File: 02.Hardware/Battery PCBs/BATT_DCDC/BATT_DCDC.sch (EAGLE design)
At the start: 66 parts, among them K3 FLEX8, Q1 NVTFS9D6P04M8LTAG, Q2 2N7002PW, Q5 2N7002PW, U1 MCP6071T-E/OT, U3 TPS55330RTET, U7 TPIC2810D

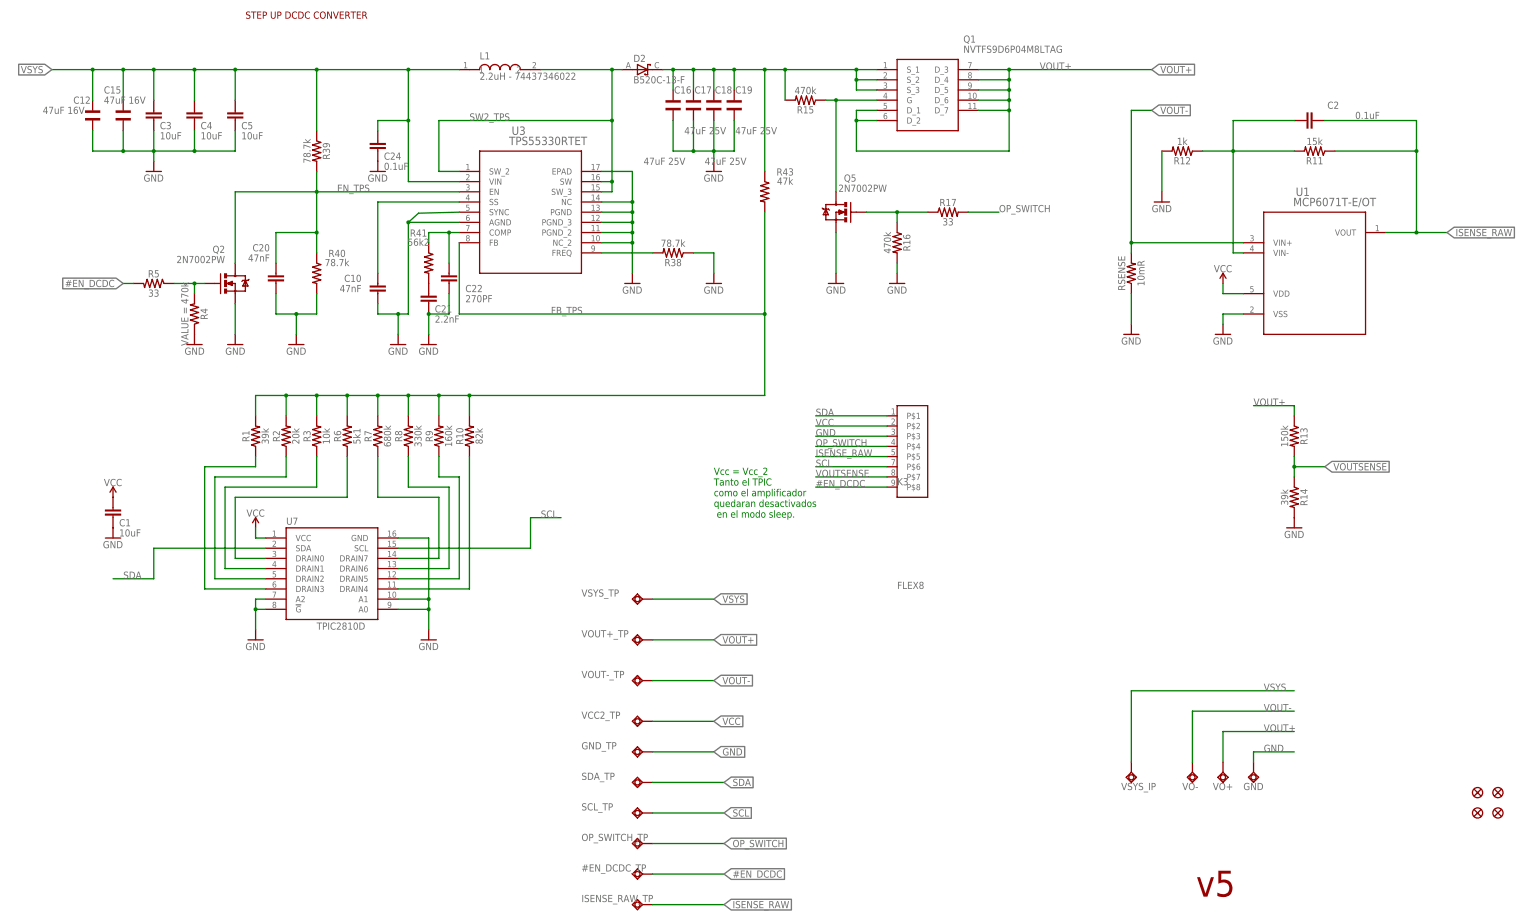
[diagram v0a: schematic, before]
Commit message: Cambios revisados con David
Revision de los pcbs de la bateria.

En el DCDC se añade un diode Clamp (bat54s) en la medicion de la tension de salida.
Actualizacion de la BOM a v8.
Documentos de Cambios de versiones
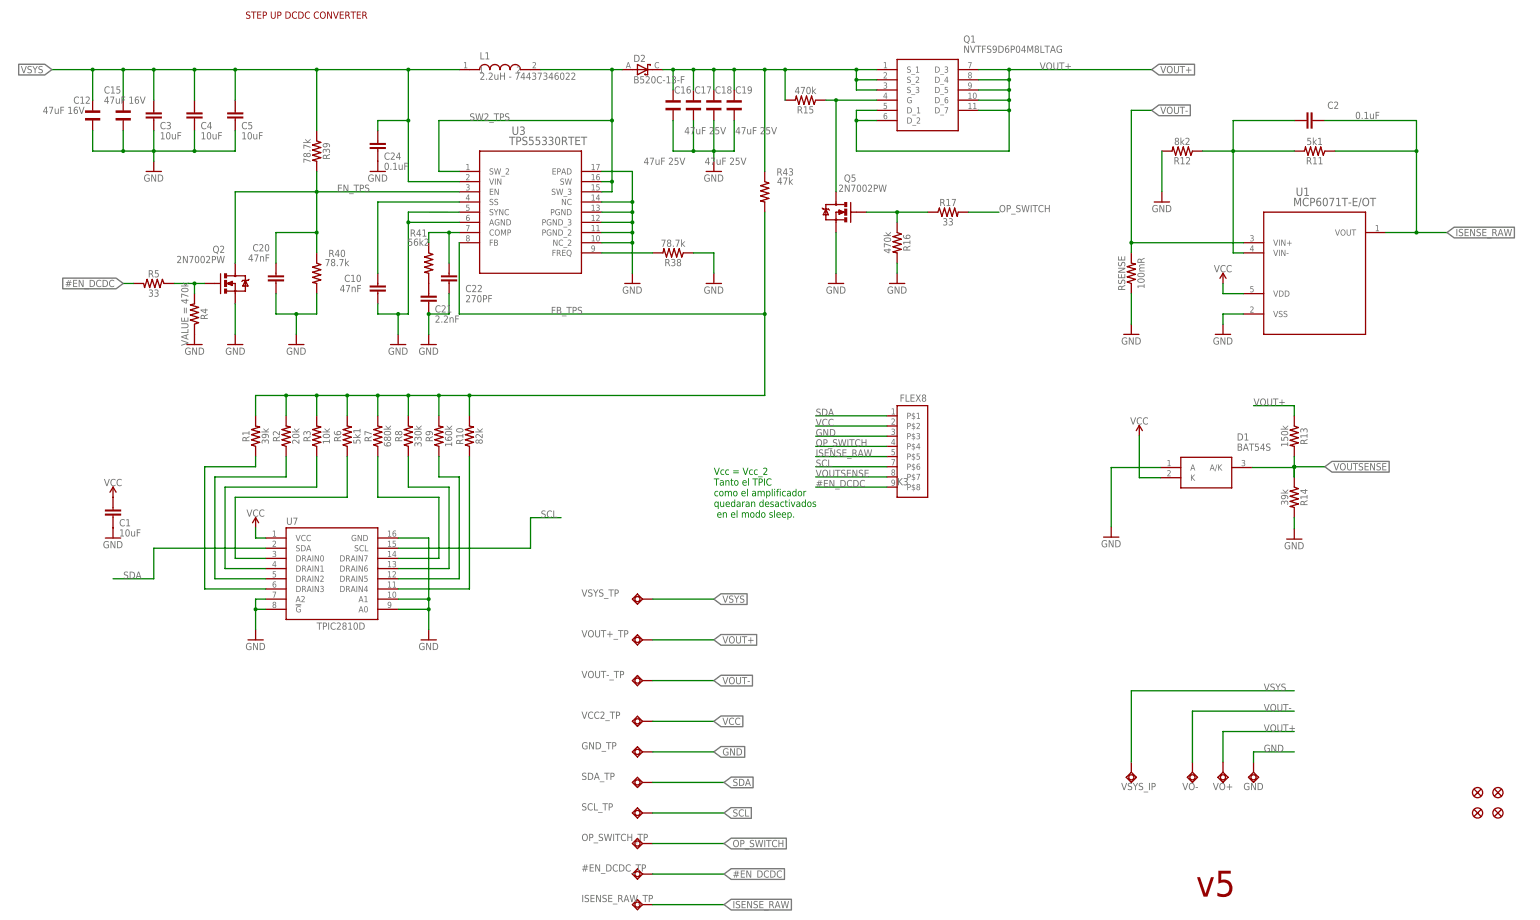
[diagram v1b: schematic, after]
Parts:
- added D1: BAT54S, BAT54S:BAT54S
- R11: value 15k -> 5k1
- R12: value 1k -> 8k2
- RSENSE: value 10mR -> 100mR
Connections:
- net GND: now also D1.A
- net VCC: now also D1.K
- net VOUTSENSE: now also D1.A/K
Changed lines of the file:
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@@
 <setting verticaltext="up"/>
 </settings>
-<grid distance="0.1" unitdist="mm" unit="mm" style="lines" multiple="1" display="no" altdistance="0.01" altunitdist="inch" altunit="inch"/>
+<grid distance="0.1" unitdist="inch" unit="inch" style="lines" multiple="1" display="no" altdistance="0.01" altunitdist="inch" altunit="inch"/>
 <layers>
 <layer number="1" name="Top" color="4" fill="1" visible="no" active="no"/>
@@
 <part name="SUPPLY2" library="SparkFun-PowerSymbols" library_urn="urn:adsk.eagle:library:530" deviceset="VCC" device=""/>
 <part name="U1" library="MCP6071" deviceset="MCP6071T-E/OT" device=""/>
-<part name="R11" library="SparkFun-Resistors" library_urn="urn:adsk.eagle:library:532" deviceset="RESISTOR" device="0402" package3d_urn="urn:adsk.eagle:package:39657/1" value="15k"/>
+<part name="R11" library="SparkFun-Resistors" library_urn="urn:adsk.eagle:library:532" deviceset="RESISTOR" device="0402" package3d_urn="urn:adsk.eagle:package:39657/1" value="5k1"/>
 <part name="FRAME2" library="microbuilder" deviceset="FRAME_A3" device=""/>
-<part name="R12" library="SparkFun-Resistors" library_urn="urn:adsk.eagle:library:532" deviceset="RESISTOR" device="0402" package3d_urn="urn:adsk.eagle:package:39657/1" value="1k"/>
+<part name="R12" library="SparkFun-Resistors" library_urn="urn:adsk.eagle:library:532" deviceset="RESISTOR" device="0402" package3d_urn="urn:adsk.eagle:package:39657/1" value="8k2"/>
 <part name="GND5" library="SparkFun" deviceset="GND" device=""/>
 <part name="C2" library="SparkFun-Capacitors" deviceset="0.1UF" device="-0603-25V-(+80/-20%)" value="0.1uF"/>
 <part name="SUPPLY3" library="SparkFun-PowerSymbols" library_urn="urn:adsk.eagle:library:530" deviceset="VCC" device=""/>
 <part name="GND6" library="SparkFun" deviceset="GND" device=""/>
-<part name="RSENSE" library="SparkFun-Resistors" library_urn="urn:adsk.eagle:library:532" deviceset="RESISTOR" device="0603" package3d_urn="urn:adsk.eagle:package:39650/1" value="10mR"/>
+<part name="RSENSE" library="SparkFun-Resistors" library_urn="urn:adsk.eagle:library:532" deviceset="RESISTOR" device="0603" package3d_urn="urn:adsk.eagle:package:39650/1" value="100mR"/>
 <part name="GND8" library="SparkFun" deviceset="GND" device=""/>
 <part name="R13" library="SparkFun-Resistors" library_urn="urn:adsk.eagle:library:532" deviceset="RESISTOR" device="0402" package3d_urn="urn:adsk.eagle:package:39657/1" value="150k"/>
@@
 <part name="VOUT+_TP" library="BeagleBone_Blue_R3" library_urn="urn:adsk.eagle:library:5828899" deviceset="TESTPAD_TPSQ" device="B1,27" package3d_urn="urn:adsk.eagle:package:5829773/2"/>
 <part name="VSYS_TP" library="BeagleBone_Blue_R3" library_urn="urn:adsk.eagle:library:5828899" deviceset="TESTPAD_TPSQ" device="B1,27" package3d_urn="urn:adsk.eagle:package:5829773/2"/>
+<part name="D1" library="BAT54S" deviceset="BAT54S" device=""/>
+<part name="GND7" library="SparkFun" deviceset="GND" device=""/>
+<part name="SUPPLY4" library="SparkFun-PowerSymbols" library_urn="urn:adsk.eagle:library:530" deviceset="VCC" device=""/>
 </parts>
 <sheets>
@@
 <attribute name="VALUE" x="323.596" y="121.92" size="1.778" layer="96" font="vector" rot="R270" align="top-center"/>
 </instance>
-<instance part="GND10" gate="1" x="325.12" y="114.3" smashed="yes">
-<attribute name="VALUE" x="322.58" y="111.76" size="1.778" layer="96"/>
+<instance part="GND10" gate="1" x="325.12" y="111.5" smashed="yes">
+<attribute name="VALUE" x="322.58" y="108.96" size="1.778" layer="96"/>
 </instance>
 <instance part="K3" gate="&gt;NAME" x="226.06" y="121.92" smashed="yes">
 <attribute name="NAME" x="226.06" y="124.92" size="1.778" layer="95"/>
-<attribute name="VALUE" x="226.06" y="99.06" size="1.778" layer="96"/>
+<attribute name="VALUE" x="226.7" y="145.77" size="1.778" layer="96"/>
 </instance>
 <instance part="GND" gate="G$1" x="314.96" y="53.34" smashed="yes">
@@
 <attribute name="NAME" x="147.32" y="97.155" size="1.778" layer="95"/>
 <attribute name="TP_SIGNAL_NAME" x="161.29" y="93.98" size="1.778" layer="97" rot="R270"/>
+</instance>
+<instance part="D1" gate="G$1" x="291.74" y="129.35" smashed="yes">
+<attribute name="NAME" x="310.79" y="136.97" size="1.778" layer="95" align="center-left"/>
+<attribute name="VALUE" x="310.79" y="134.43" size="1.778" layer="96" align="center-left"/>
+</instance>
+<instance part="GND7" gate="1" x="279.46" y="111.99" smashed="yes">
+<attribute name="VALUE" x="276.92" y="109.45" size="1.778" layer="96"/>
+</instance>
+<instance part="SUPPLY4" gate="G$1" x="286.47" y="137.28" smashed="yes">
+<attribute name="VALUE" x="286.47" y="140.074" size="1.778" layer="96" align="bottom-center"/>
 </instance>
 </instances>
@@
 <junction x="101.6" y="167.64"/>
 <pinref part="U3" gate="A" pin="SYNC"/>
-<wire x1="116.84" y1="193.04" x2="106.68" y2="192.786" width="0.1524" layer="91"/>
-<wire x1="106.68" y1="192.786" x2="104.14" y2="190.5" width="0.1524" layer="91"/>
+<wire x1="116.84" y1="193.04" x2="104.14" y2="193.056" width="0.1524" layer="91"/>
+<wire x1="104.14" y1="193.056" x2="104.14" y2="190.5" width="0.1524" layer="91"/>
 <junction x="104.14" y="190.5"/>
 </segment>
@@
 <pinref part="R14" gate="G$1" pin="2"/>
 <pinref part="GND10" gate="1" pin="GND"/>
+<wire x1="325.12" y1="114.04" x2="325.12" y2="116.84" width="0.1524" layer="91"/>
 </segment>
 <segment>
@@
 <label x="205.74" y="137.16" size="1.778" layer="95"/>
 <pinref part="K3" gate="&gt;NAME" pin="P$3"/>
+</segment>
+<segment>
+<pinref part="GND7" gate="1" pin="GND"/>
+<pinref part="D1" gate="G$1" pin="A"/>
+<wire x1="291.74" y1="129.35" x2="279.46" y2="129.35" width="0.1524" layer="91"/>
+<wire x1="279.46" y1="129.35" x2="279.46" y2="114.53" width="0.1524" layer="91"/>
 </segment>
 </net>
@@
 <pinref part="K3" gate="&gt;NAME" pin="P$2"/>
 </segment>
+<segment>
+<pinref part="SUPPLY4" gate="G$1" pin="VCC"/>
+<pinref part="D1" gate="G$1" pin="K"/>
+<wire x1="291.74" y1="126.81" x2="286.47" y2="126.81" width="0.1524" layer="91"/>
+<wire x1="286.47" y1="126.81" x2="286.47" y2="137.28" width="0.1524" layer="91"/>
+</segment>
 </net>
 <net name="N$1" class="0">
@@
 <junction x="325.12" y="129.54"/>
 <label x="332.74" y="129.54" size="1.778" layer="95" xref="yes"/>
-</segment>
-<segment>
+<pinref part="D1" gate="G$1" pin="A/K"/>
+<wire x1="314.6" y1="129.35" x2="325.12" y2="129.35" width="0.1524" layer="91"/>
+<wire x1="325.12" y1="129.35" x2="325.12" y2="127" width="0.1524" layer="91"/>
+<junction x="325.12" y="129.5"/>
+</segment>
+<segment>

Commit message: Review final antes de produccion
-cambian valores de c10, r13, r15
-se añaden notas
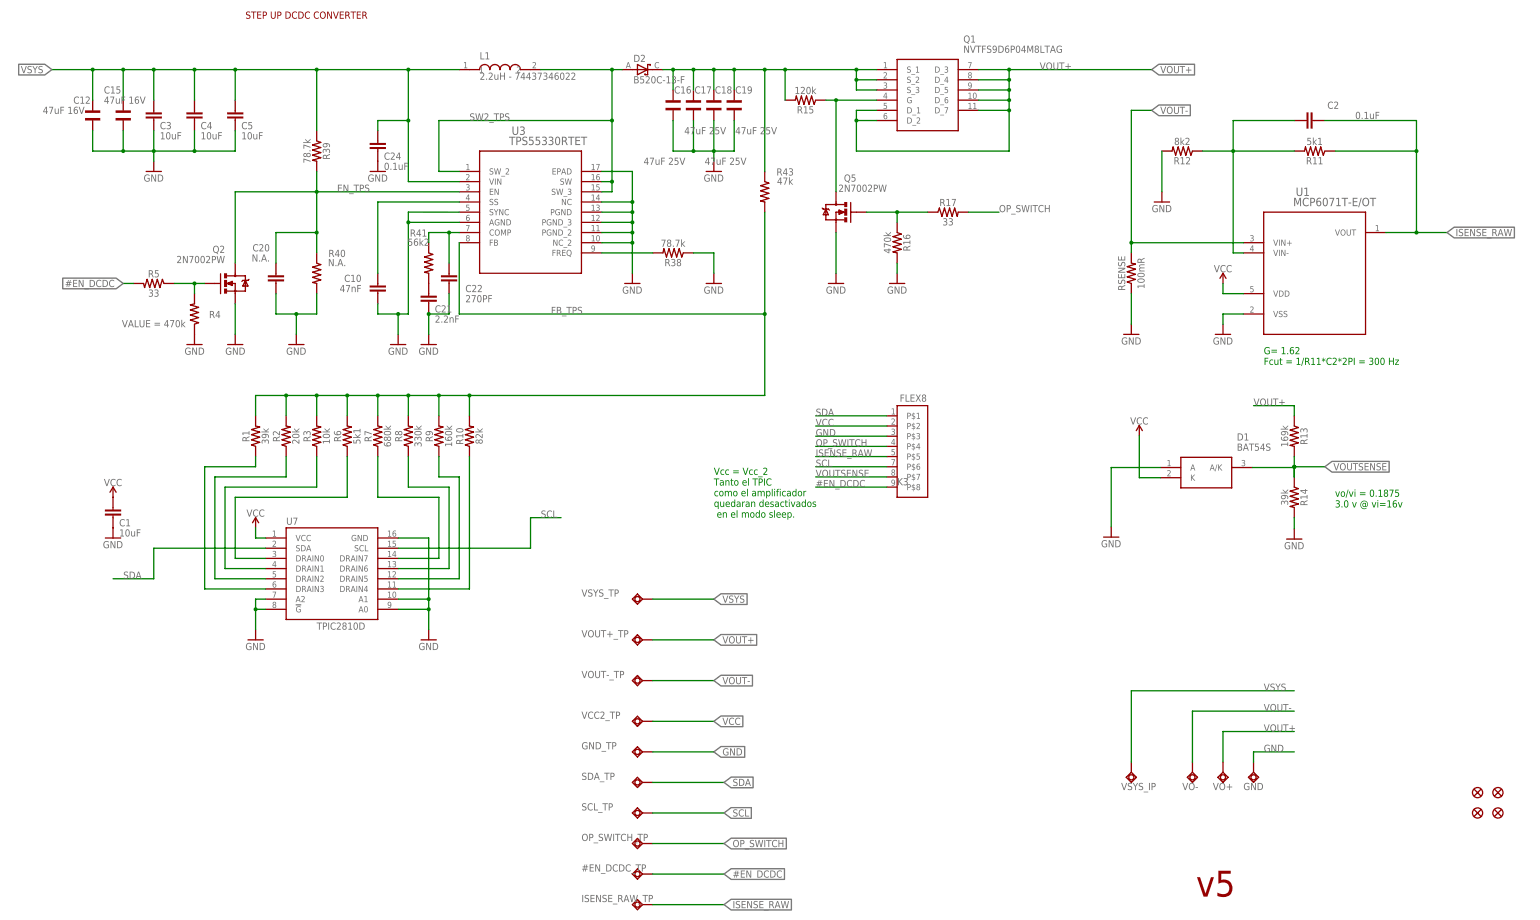
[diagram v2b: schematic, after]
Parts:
- C20: value 47nF -> N.A.
- R13: value 150k -> 169k
- R15: value 470k -> 120k
- R40: value 78.7k -> N.A.
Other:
- note added: "G= 1.62 Fcut = 1/R11*C2*2PI = 300 Hz"
- note added: "vo/vi = 0.1875 3.0 v @ vi=16v"
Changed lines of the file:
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@@
 <part name="GND28" library="SparkFun" deviceset="GND" device=""/>
 <part name="R39" library="SparkFun-Resistors" library_urn="urn:adsk.eagle:library:532" deviceset="RESISTOR" device="0402" package3d_urn="urn:adsk.eagle:package:39657/1" value="78.7k"/>
-<part name="R40" library="SparkFun-Resistors" library_urn="urn:adsk.eagle:library:532" deviceset="RESISTOR" device="0402" package3d_urn="urn:adsk.eagle:package:39657/1" value="78.7k"/>
-<part name="C20" library="SparkFun-Capacitors" deviceset="47NF" device="-0603-25V-5%" value="47nF"/>
+<part name="R40" library="SparkFun-Resistors" library_urn="urn:adsk.eagle:library:532" deviceset="RESISTOR" device="0402" package3d_urn="urn:adsk.eagle:package:39657/1" value="N.A."/>
+<part name="C20" library="SparkFun-Capacitors" deviceset="47NF" device="-0603-25V-5%" value="N.A."/>
 <part name="GND29" library="SparkFun" deviceset="GND" device=""/>
 <part name="C21" library="SparkFun-Capacitors" deviceset="2.2NF/2200PF" device="-0603-50V-10%" value="2.2nF"/>
@@
 <part name="R10" library="SparkFun-Resistors" library_urn="urn:adsk.eagle:library:532" deviceset="RESISTOR" device="0402" package3d_urn="urn:adsk.eagle:package:39657/1" value="82k"/>
 <part name="Q1" library="SamacSys_Parts" deviceset="NVTFS9D6P04M8LTAG" device=""/>
-<part name="R15" library="SparkFun-Resistors" library_urn="urn:adsk.eagle:library:532" deviceset="RESISTOR" device="0402" package3d_urn="urn:adsk.eagle:package:39657/1" value="470k"/>
+<part name="R15" library="SparkFun-Resistors" library_urn="urn:adsk.eagle:library:532" deviceset="RESISTOR" device="0402" package3d_urn="urn:adsk.eagle:package:39657/1" value="120k"/>
 <part name="R16" library="SparkFun-Resistors" library_urn="urn:adsk.eagle:library:532" deviceset="RESISTOR" device="0402" package3d_urn="urn:adsk.eagle:package:39657/1" value="470k"/>
 <part name="R17" library="SparkFun-Resistors" library_urn="urn:adsk.eagle:library:532" deviceset="RESISTOR" device="0402" package3d_urn="urn:adsk.eagle:package:39657/1" value="33"/>
@@
 <part name="RSENSE" library="SparkFun-Resistors" library_urn="urn:adsk.eagle:library:532" deviceset="RESISTOR" device="0603" package3d_urn="urn:adsk.eagle:package:39650/1" value="100mR"/>
 <part name="GND8" library="SparkFun" deviceset="GND" device=""/>
-<part name="R13" library="SparkFun-Resistors" library_urn="urn:adsk.eagle:library:532" deviceset="RESISTOR" device="0402" package3d_urn="urn:adsk.eagle:package:39657/1" value="150k"/>
+<part name="R13" library="SparkFun-Resistors" library_urn="urn:adsk.eagle:library:532" deviceset="RESISTOR" device="0402" package3d_urn="urn:adsk.eagle:package:39657/1" value="169k"/>
 <part name="R14" library="SparkFun-Resistors" library_urn="urn:adsk.eagle:library:532" deviceset="RESISTOR" device="0402" package3d_urn="urn:adsk.eagle:package:39657/1" value="39k"/>
 <part name="GND10" library="SparkFun" deviceset="GND" device=""/>
@@
  en el modo sleep.</text>
 <text x="300.62" y="22.32" size="6.4516" layer="94">v5</text>
+<text x="317.5" y="154.94" size="1.778" layer="91">G= 1.62
+Fcut = 1/R11*C2*2PI = 300 Hz</text>
+<text x="335.28" y="119.38" size="1.778" layer="91">vo/vi = 0.1875
+3.0 v @ vi=16v</text>
 </plain>
 <instances>
@@
 </instance>
 <instance part="R4" gate="G$1" x="50.8" y="167.64" smashed="yes" rot="MR90">
-<attribute name="NAME" x="52.324" y="167.64" size="1.778" layer="95" font="vector" rot="MR90" align="bottom-center"/>
-<attribute name="VALUE" x="49.276" y="167.64" size="1.778" layer="96" font="vector" rot="MR90" align="top-center" display="both"/>
+<attribute name="NAME" x="55.88" y="166.624" size="1.778" layer="95" font="vector" rot="MR0" align="bottom-center"/>
+<attribute name="VALUE" x="40.64" y="166.116" size="1.778" layer="96" font="vector" rot="MR0" align="top-center" display="both"/>
 </instance>
 <instance part="R5" gate="G$1" x="40.64" y="175.26" smashed="yes" rot="MR0">
